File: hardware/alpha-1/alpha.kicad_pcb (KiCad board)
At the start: 2 copper layers, 65 x 56 mm, 77 parts, among them J1 POWER, J2 SERIAL, P1 OUTPUTS, P7 INPUTS, P9 12V, Q1 DMN2041L-7, Q2 DMN2041L-7, Q3 DMN2041L-7, Q4 DMN2041L-7, Q5 DMN2041L-7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

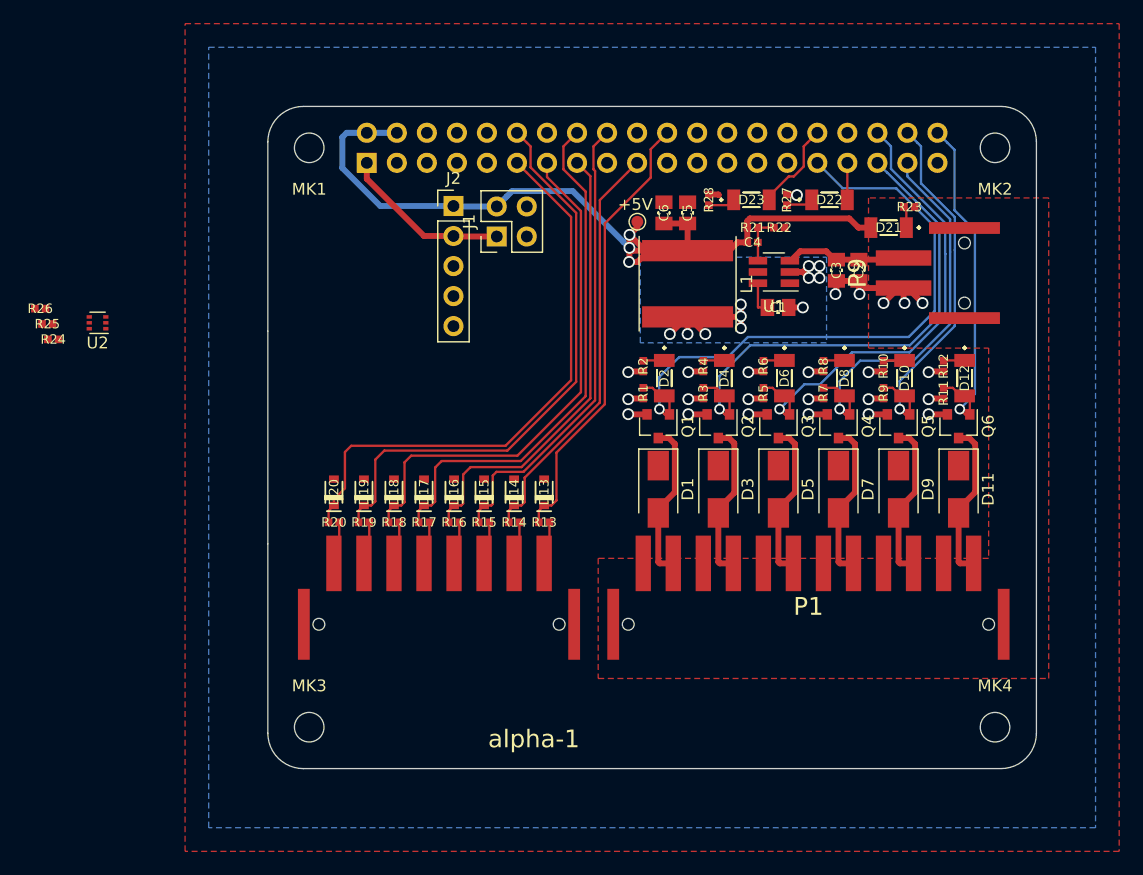
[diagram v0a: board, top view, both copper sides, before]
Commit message: o Routing complete. o Adding some print. o Milling out area around TMP102.
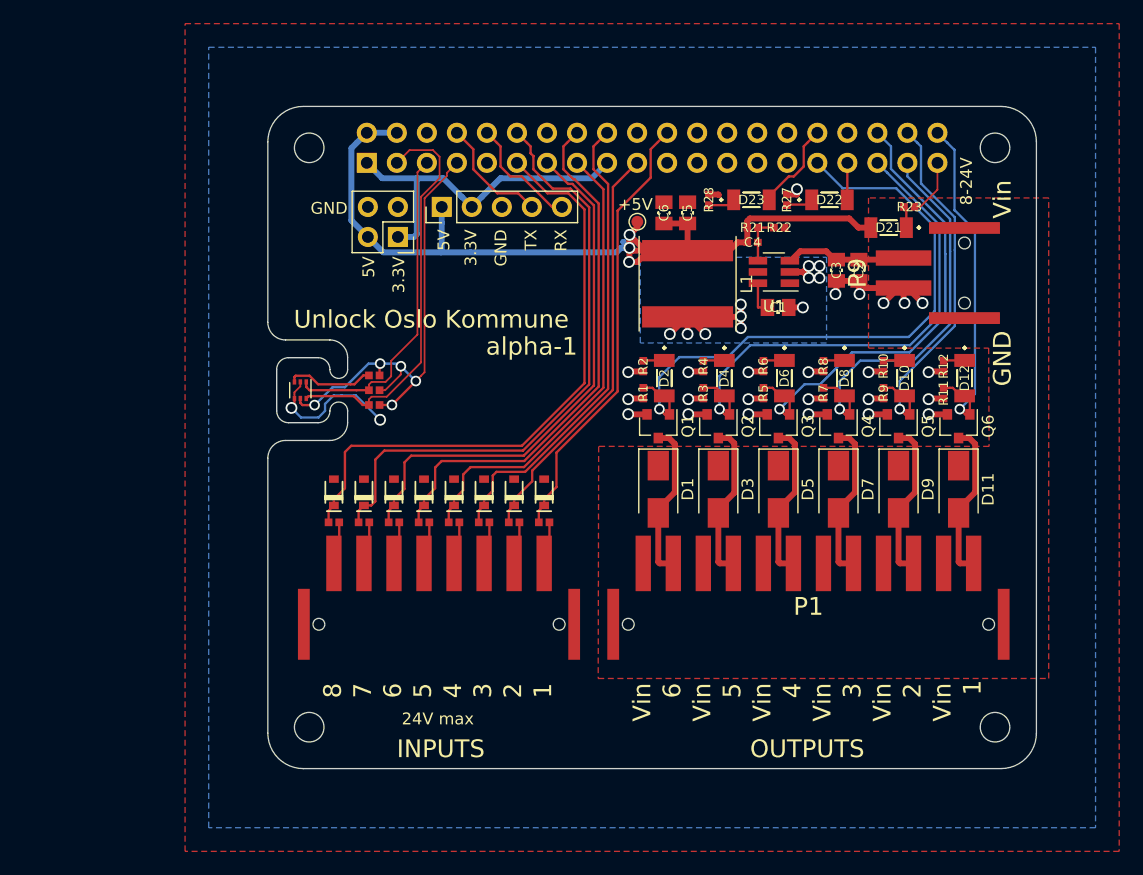
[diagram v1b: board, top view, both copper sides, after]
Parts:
- moved R26 28.8 mm to (209.0, 116.8), turned to 180 degrees
- moved R25 28.5 mm to (209.0, 119.2), turned to 180 degrees
- moved R24 27.5 mm to (209.0, 118.0)
- moved U2 18.1 mm to (202.8, 118.0), turned to 270 degrees
- moved J1 8.36 mm to (211.0, 105.0), turned to 180 degrees
- moved J2 0.99 mm to (214.7, 102.5), turned to 90 degrees
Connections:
- net Net-(R26-Pad2) renamed /~TMP102_ALERT
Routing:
- net /TMP102_PWR: track 0.00 -> 40.2 mm, vias 0 -> 5
- net /TMP102_SDA: track 0.00 -> 34.2 mm
- net /TMP102_SCL: track 0.00 -> 27.8 mm
- net GND: track 40.7 -> 58.2 mm, vias 24 -> 26
- net +3V3: track 14.4 -> 29.8 mm
- net /SERIAL_TX: track 0.00 -> 9.93 mm
- net /SERIAL_RX: track 0.00 -> 9.93 mm
- net /~TMP102_ALERT: track 0.00 -> 7.38 mm
- net +5V: track 77.4 -> 81.7 mm
- net /INPUT_8: track 48.4 -> 51.2 mm
- net /INPUT_7: track 49.1 -> 51.7 mm
- net /INPUT_6: track 43.9 -> 45.0 mm
- net /INPUT_5: track 44.3 -> 45.1 mm
- net /INPUT_4: track 38.7 -> 39.4 mm
- net /INPUT_3: track 39.3 -> 39.9 mm
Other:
- outline, holes or cut-outs redrawn
- net class Default: clearance 0.2 -> 0.15; trace_width 0.2 -> 0.15
- rule trace_clearance: 0.2 -> 0.15
- rule trace_min: 0.1524 -> 0.15
- board text added: "1"
- board text added: "2"
- board text added: "24V max"
- board text added: "3"
- board text added: "3.3V"
- board text added: "4"
- board text added: "5"
- board text added: "5V"
- board text added: "6"
- board text added: "7"
- board text added: "8"
- board text added: "8-24V"
- board text added: "GND"
- board text added: "INPUTS"
- board text added: "OUTPUTS"
- board text added: "RX"
- board text added: "TX"
- board text added: "Unlock Oslo Kommune"
- board text added: "Vin"

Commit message: o Some silk screen improvements.
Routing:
- net +5V: track 81.7 -> 81.0 mm
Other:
- net class Default: via_dia 0.9 -> 0.6; via_drill 0.6 -> 0.3
- net class Power: via_dia 1 -> 0.6; via_drill 0.7 -> 0.3
- rule via_min_drill: 0.5 -> 0.25
- rule via_min_size: 0.8 -> 0.6
- board text added: "Unlock Oslo kommune!"
- board text removed: "Unlock Oslo Kommune"

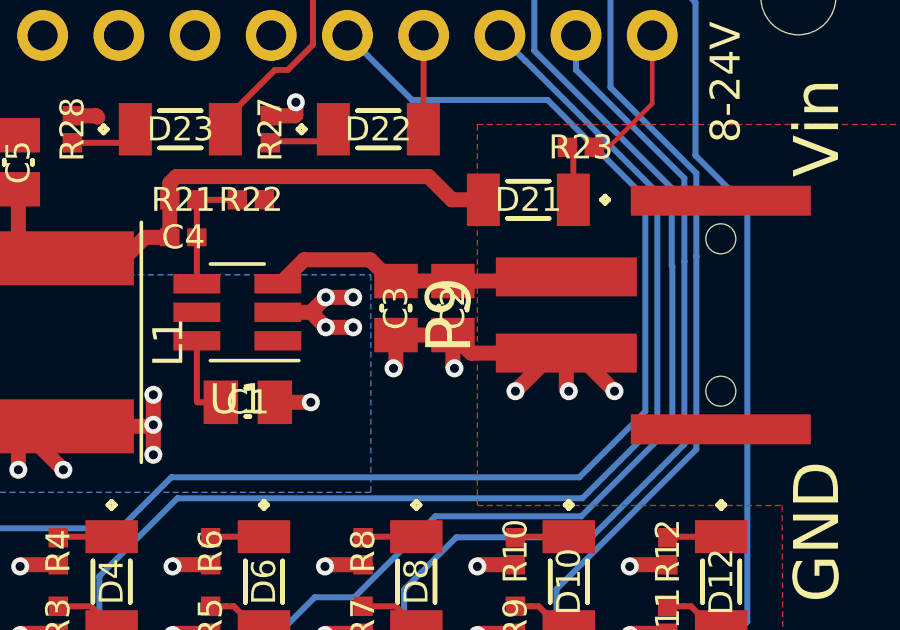
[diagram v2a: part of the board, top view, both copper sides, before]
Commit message: o Fixing the rest of the missing components. o Ready for production.
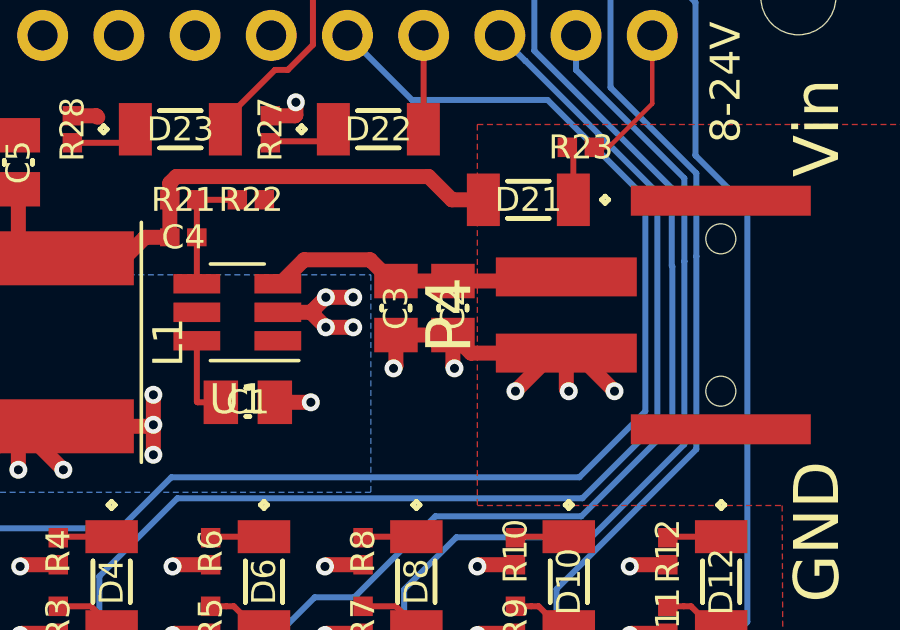
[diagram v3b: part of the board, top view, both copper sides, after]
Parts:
- renumbered P7 to P2, U3 to P3, P9 to P4

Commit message: hardware: Add reverse polarity protection and fix output silkscreen
Using a SOD-123 (MINISMA) diode like
https://www.digikey.no/product-detail/en/comchip-technology/CDBM140-G/641-1325-1-ND/1979690

Note: Using Kicad5, might not be compatible with KiCad4 anymore
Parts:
- added D24: CDBM140-G, Diodes_SMD:D_SOD-123, F.Cu at (249.6, 107.2)
- moved C2 3.58 mm to (250.4, 111.4)
- moved C3 3.58 mm to (248.5, 111.4)
- moved R23 2.54 mm to (256.7, 101.7), turned to 90 degrees
- moved D21 2.41 mm to (252.7, 101.9)
- moved P4 1.35 mm to (259.5, 108.5)
- moved C1 1.14 mm to (243.2, 112.1)
- moved U1 1.14 mm to (242.8, 109.1)
- moved R22 0.27 mm to (243.2, 104.5)
- moved R21 0.14 mm to (241.0, 104.4)
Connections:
- P4 pad 1: Vin -> Net-(D24-Pad2)
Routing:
- net GND: track 58.2 -> 50.4 mm, vias 26 -> 21
- net Net-(D24-Pad2): track 0.00 -> 3.86 mm
- net +5V: track 81.0 -> 82.8 mm
- net /FB: track 4.15 -> 5.16 mm
- net Vin: track 10.3 -> 11.1 mm
- net Net-(D21-Pad1): track 1.83 -> 2.57 mm
- net /SWITCH_6: track 30.1 -> 30.4 mm, vias 1 -> 2
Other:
- board text added: "alpha-1.1"
- board text removed: "alpha-1"
